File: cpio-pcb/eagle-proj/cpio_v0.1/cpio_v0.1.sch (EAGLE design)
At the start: 2 parts

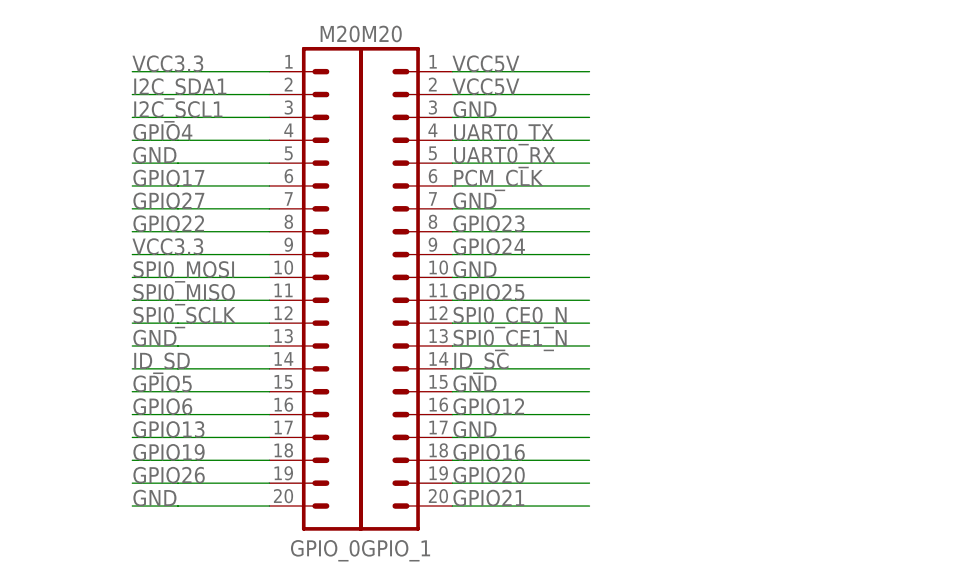
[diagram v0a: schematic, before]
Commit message: schematic update
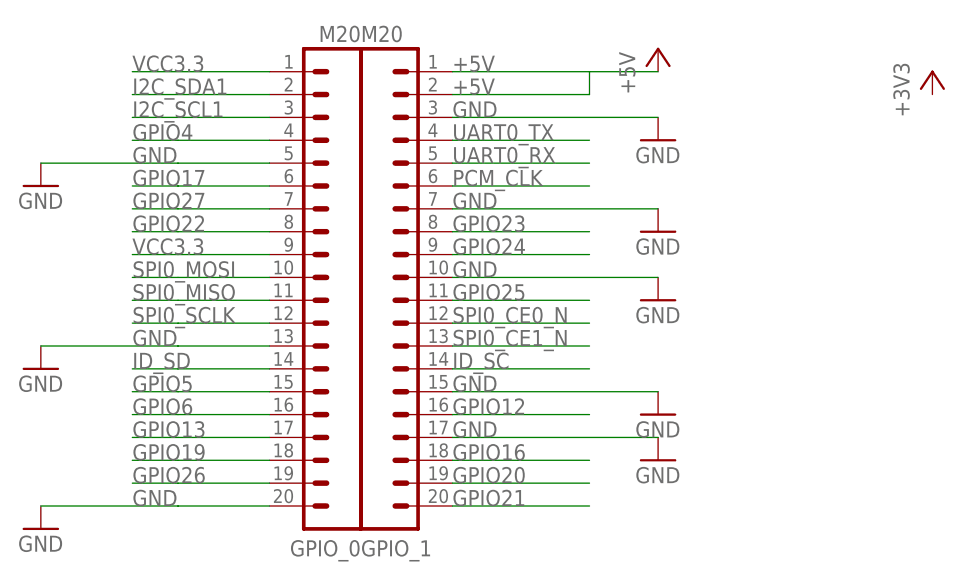
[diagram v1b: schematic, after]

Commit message: clean start with components population of Eagle library
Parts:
- removed GPIO_0, GPIO_1: M20, SparkFun-Connectors:M20
- added JP1: M20X2, SparkFun-Connectors:M20X2
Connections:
- removed net VCC3.3: GPIO_0.1
- new net +5V: JP1.2, JP1.4
- new net GND: JP1.14, JP1.20, JP1.30, JP1.34, JP1.6
- new net GPIO12: JP1.32
- new net GPIO16: JP1.36
- new net GPIO20: JP1.38
- new net GPIO21: JP1.40
- new net GPIO23: JP1.16
- new net GPIO24: JP1.18
- new net GPIO25: JP1.22
- new net ID_SC: JP1.28
- new net PCM_CLK: JP1.12
- new net SPI0_CE0_N: JP1.24
- new net SPI0_CE1_N: JP1.26
- new net UART0_RX: JP1.10
- new net UART0_TX: JP1.8

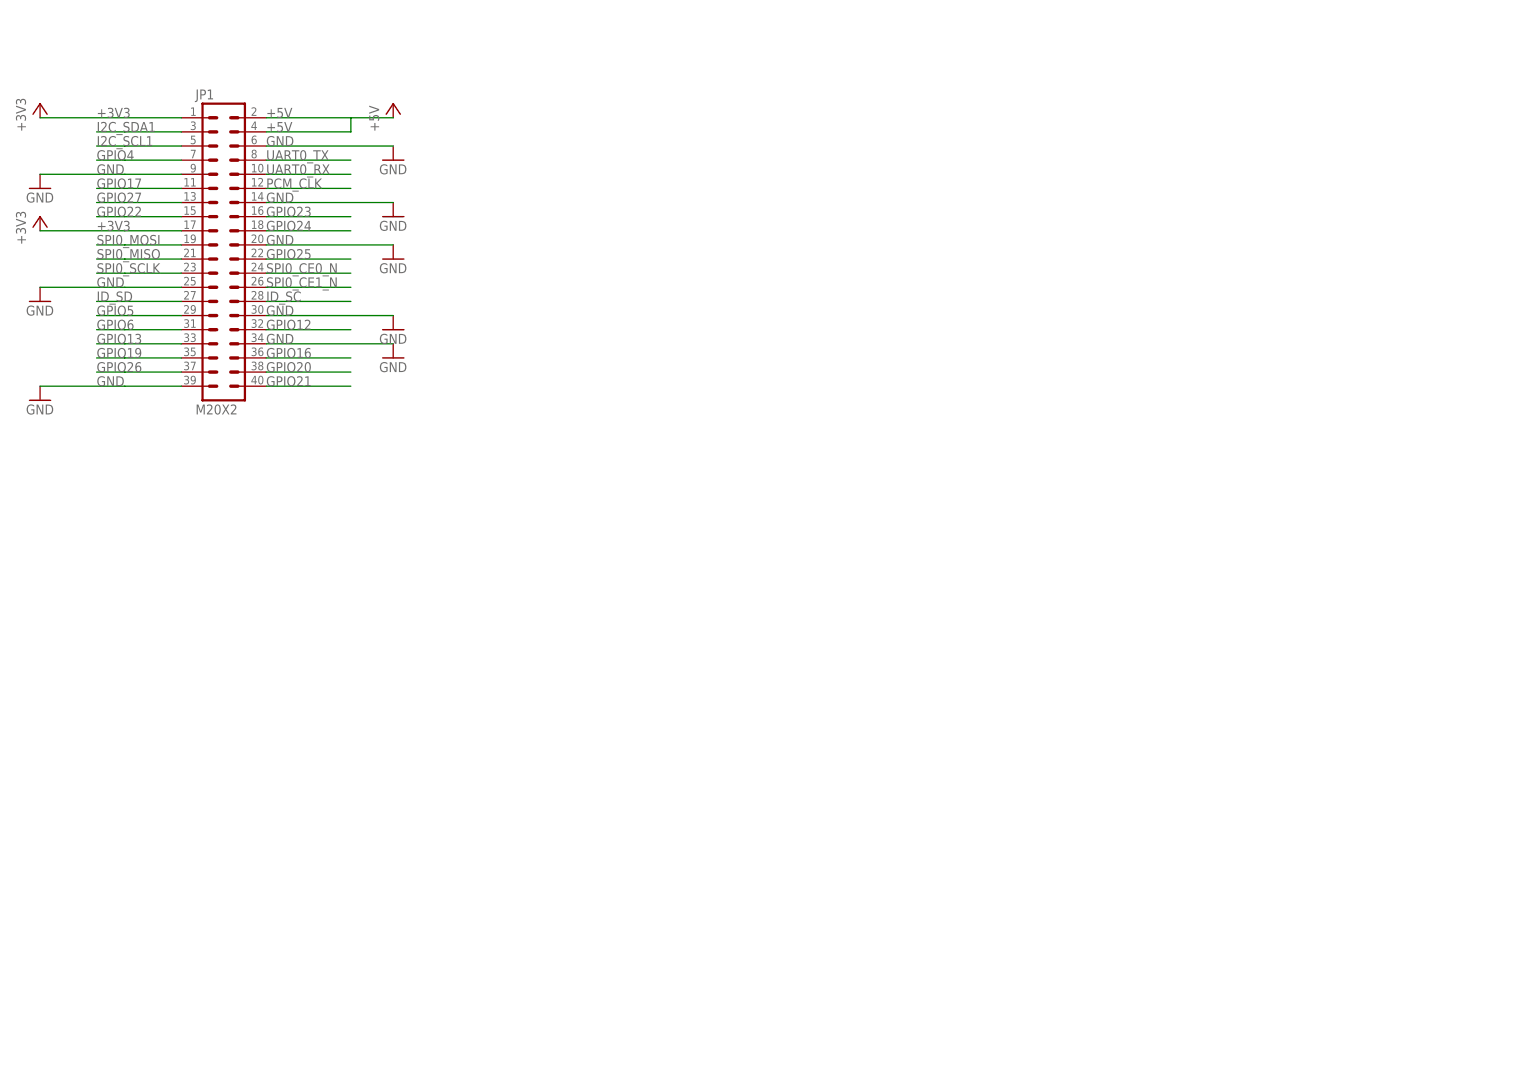
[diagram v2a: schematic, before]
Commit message: schematic for power domains done
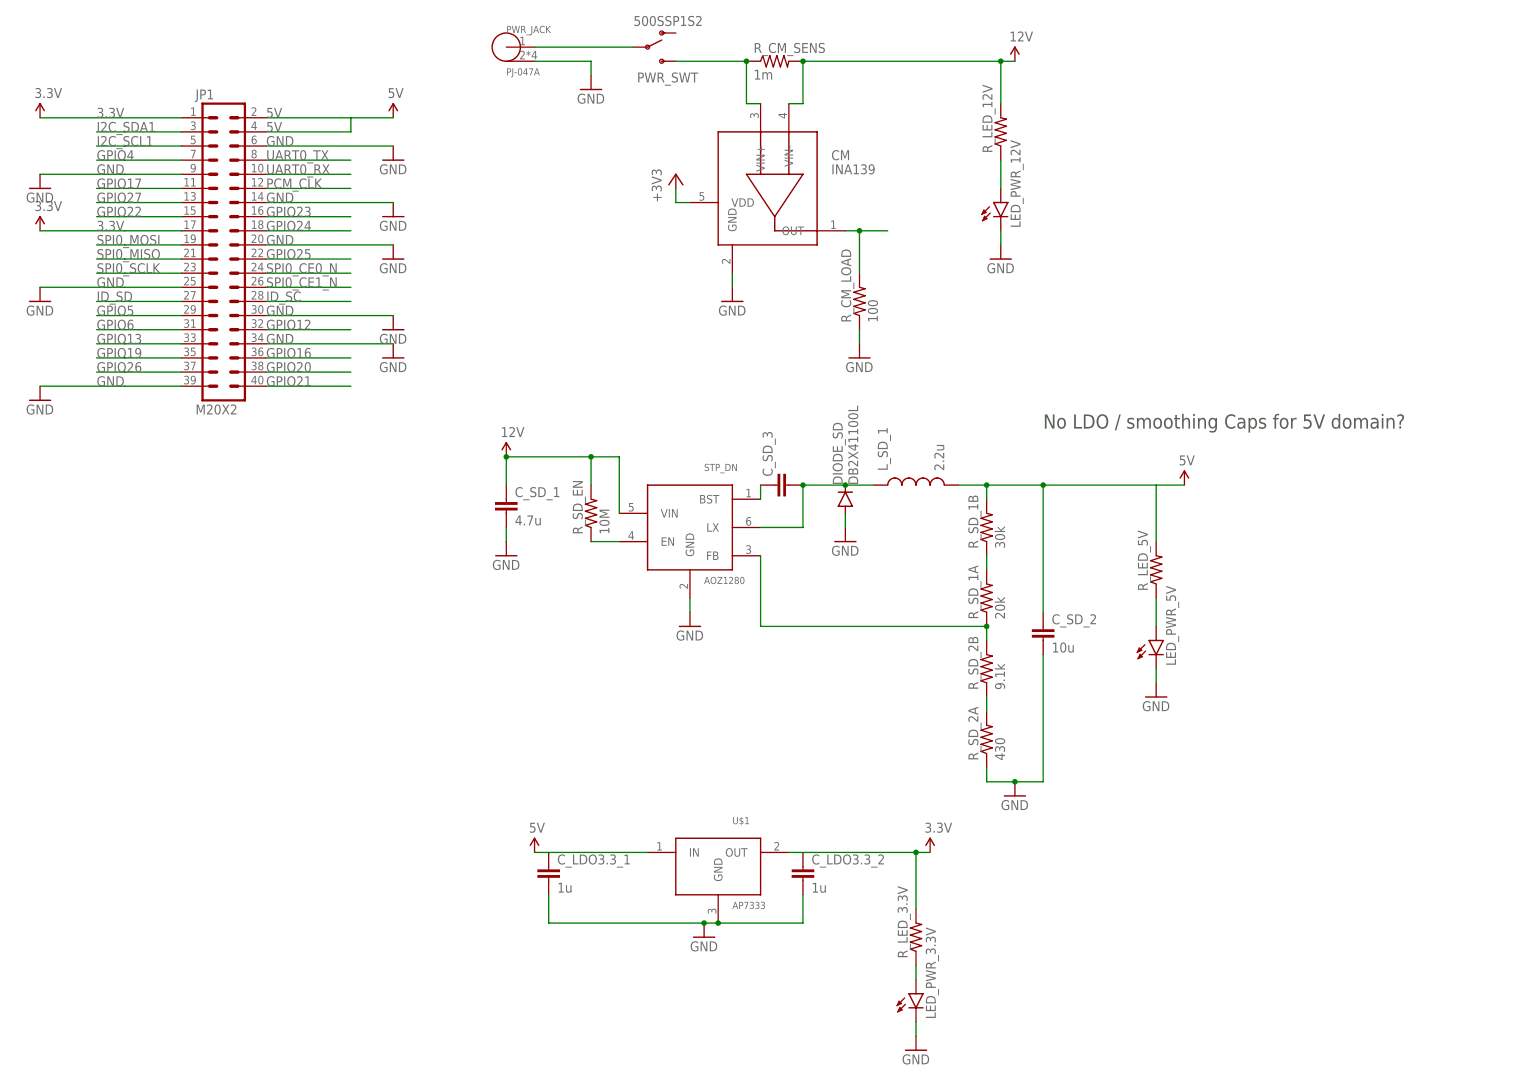
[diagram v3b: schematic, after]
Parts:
- added CM: INA139, cpio:INA139
- added C_LDO3.3_1, C_LDO3.3_2: 1u, SparkFun-Passives:CAP0805
- added C_SD_1: 4.7u, SparkFun-Passives:CAP0805
- added C_SD_2: 10u, SparkFun-Passives:CAP0805
- added C_SD_3: (no value), SparkFun-Passives:CAP0805
- added DIODE_SD: DB2X41100L, cpio:DB2X41100L
- added LED_PWR_12V, LED_PWR_3.3V, LED_PWR_5V: (no value), SparkFun-LED:LED1206
- added L_SD_1: 2.2u, SparkFun-Passives:INDUCTOR0805
- added PWR_JACK: PJ-047A, cpio:PJ-047A
- added PWR_SWT: 500SSP1S2, cpio:500SSP1S2
- added R_CM_LOAD: 100, SparkFun-Passives:RESISTOR0805-RES
- added R_CM_SENS: 1m, SparkFun-Passives:RESISTOR0805-RES
- added R_LED_12V, R_LED_3.3V, R_LED_5V: (no value), SparkFun-Passives:RESISTOR0805-RES
- added R_SD_1A: 20k, SparkFun-Passives:RESISTOR0805-RES
- added R_SD_1B: 30k, SparkFun-Passives:RESISTOR0805-RES
- added R_SD_2A: 430, SparkFun-Passives:RESISTOR0805-RES
- added R_SD_2B: 9.1k, SparkFun-Passives:RESISTOR0805-RES
- added R_SD_EN: 10M, SparkFun-Passives:RESISTOR0805-RES
- added STP_DN: AOZ1280, cpio:AOZ1280
- added U$1: AP7333, cpio:AP7333
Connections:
- removed net +5V: JP1.2, JP1.4
- new net +3V3: CM.VDD
- new net 12V: CM.VIN-, C_SD_1.1, R_CM_SENS.2, R_LED_12V.2, R_SD_EN.2, STP_DN.VIN
- new net 3.3V: R_LED_3.3V.2, U$1.OUT
- new net 5V: C_SD_2.1, JP1.2, JP1.4, L_SD_1.2, R_SD_1B.2, U$1.IN
- new net N$10: C_SD_3.2, DIODE_SD.C, L_SD_1.1, STP_DN.LX
- new net N$11: LED_PWR_5V.A, R_LED_5V.1
- new net N$12: R_SD_1A.1, R_SD_2B.2, STP_DN.FB
- new net N$13: R_SD_2A.2, R_SD_2B.1
- new net N$15: LED_PWR_3.3V.A, R_LED_3.3V.1
- new net N$2: LED_PWR_12V.A, R_LED_12V.1
- new net N$3: PWR_JACK.PWR, PWR_SWT.2
- new net N$4: CM.OUT, R_CM_LOAD.2
- new net N$5: CM.VIN+, PWR_SWT.3, R_CM_SENS.1
- new net N$6: R_SD_EN.1, STP_DN.EN
- new net N$7: R_LED_5V.2
- new net N$8: C_SD_3.1, STP_DN.BST
- new net N$9: R_SD_1A.2, R_SD_1B.1
- net GND: now also CM.GND, C_LDO3.3_1.2, C_LDO3.3_2.2, C_SD_1.2, C_SD_2.2, DIODE_SD.A, LED_PWR_12V.C, LED_PWR_3.3V.C, LED_PWR_5V.C, PWR_JACK.GND, R_CM_LOAD.1, R_SD_2A.1, STP_DN.GND, U$1.GND
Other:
- note added: "No LDO / smoothing Caps for 5V domain?"

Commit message: larger PCB schematic updated, onlyUI missing
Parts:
- added ADC: ADS1115, cpio:ADS1115
- added CAMERA: XH-A-6, cpio:XH-A-6
- added C_ADC: 100n, SparkFun-Passives:CAP0805
- added HEAT_0, HEAT_1, HEAT_2, HEAT_3, SENS_BRIGHT: XH-A-2, cpio:XH-A-2
- added R_1WIRE: 4.7k, SparkFun-Passives:RESISTOR0805-RES
- added R_BRIGHT: (no value), SparkFun-Passives:RESISTOR0805-RES
- added R_HSS_GND, R_SS_PROT0, R_SS_PROT1, R_SS_PROT2, R_SS_PROT3: 1k, SparkFun-Passives:RESISTOR0805-RES
- added R_HSS_PROT_0, R_HSS_PROT_1, R_HSS_PROT_2, R_HSS_PROT_3, R_HSS_SD, R_I2C_0, R_I2C_1, R_SPI_0, R_SPI_1, R_SPI_2, R_SPI_3: 10k, SparkFun-Passives:RESISTOR0805-RES
- added SENS_HUM_0, SENS_HUM_1: XH-A-4, cpio:XH-A-4
- added SENS_TEMP_0, SENS_TEMP_1, SENS_TEMP_2, SENS_TEMP_3: XH-A-3, cpio:XH-A-3
- added SWT_HEAT: VNQ5E160K-E, cpio:VNQ5E160K-E
- added SWT_SENS: 74CBTLV3125, cpio:74CBTLV3125
- renumbered PWR_SWT to SWT_PWR
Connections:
- removed net PCM_CLK: JP1.12
- new net 1WIRE: JP1.12, R_1WIRE.1, SENS_TEMP_0.2, SENS_TEMP_1.2, SENS_TEMP_2.2, SENS_TEMP_3.2
- new net ADC_BRIGHT: ADC.AIN1, R_BRIGHT.1
- new net ADC_PWR: ADC.AIN0, CM.OUT, R_CM_LOAD.2
- new net I2C_SCL: ADC.SCL, R_I2C_0.1, SENS_HUM_0.2, SENS_HUM_1.2
- new net I2C_SDA: ADC.SDA, R_I2C_1.1, SENS_HUM_0.3, SENS_HUM_1.3
- new net N$1: JP1.11, JP1.13, JP1.15, JP1.19, JP1.21, JP1.23, JP1.25, JP1.27, JP1.29, JP1.3, JP1.31, JP1.33, JP1.35, JP1.37, JP1.39, JP1.5, JP1.7, JP1.9
- new net N$14: R_SS_PROT0.2, SWT_SENS.1OE
- new net N$16: SENS_TEMP_1.1, SWT_SENS.2B
- new net N$17: SENS_TEMP_0.1, SWT_SENS.1B
- new net N$18: SENS_TEMP_2.1, SWT_SENS.3B
- new net N$19: SENS_TEMP_3.1, SWT_SENS.4B
- new net N$20: R_SS_PROT1.2, SWT_SENS.2OE
- new net N$21: R_SS_PROT2.2, SWT_SENS.3OE
- new net N$22: R_SS_PROT3.2, SWT_SENS.4OE
- new net N$24: ADC.AIN2
- new net N$25: ADC.AIN3
- new net N$26: HEAT_2.1, SWT_HEAT.OUTPUT3
- new net N$27: HEAT_1.1, SWT_HEAT.OUTPUT2
- new net N$28: HEAT_0.1, SWT_HEAT.OUTPUT1
- new net N$29: HEAT_3.1, SWT_HEAT.OUTPUT4
- new net N$30: R_HSS_SD.1, SWT_HEAT.STAT_DIS
- new net N$31: R_HSS_PROT_3.2, SWT_HEAT.INPUT4
- new net N$32: R_HSS_PROT_2.2, SWT_HEAT.INPUT3
- new net N$33: R_HSS_PROT_1.2, SWT_HEAT.INPUT2
- new net N$34: R_HSS_PROT_0.2, SWT_HEAT.INPUT1
- new net N$35: R_BRIGHT.2, SENS_BRIGHT.1
- new net SPI0_MISO: CAMERA.4, R_SPI_1.1
- new net SPI0_MOSI: CAMERA.3, R_SPI_2.1
- new net SPI0_SCLK: CAMERA.2, R_SPI_0.1
- net 12V: now also SWT_HEAT.VCC
- net 3.3V: now also ADC.VDD, CAMERA.1, C_ADC.2, JP1.1, JP1.17, R_1WIRE.2, R_HSS_SD.2, R_I2C_0.2, R_I2C_1.2, R_SPI_0.2, R_SPI_1.2, R_SPI_2.2, R_SPI_3.2, SENS_HUM_0.1, SENS_HUM_1.1, SWT_SENS.1A, SWT_SENS.2A, SWT_SENS.3A, SWT_SENS.4A, SWT_SENS.VCC
- net GND: now also ADC.ADDR, ADC.GND, CAMERA.6, C_ADC.1, HEAT_0.2, HEAT_1.2, HEAT_2.2, HEAT_3.2, R_HSS_GND.2, SENS_BRIGHT.2, SENS_HUM_0.4, SENS_HUM_1.4, SENS_TEMP_0.3, SENS_TEMP_1.3, SENS_TEMP_2.3, SENS_TEMP_3.3, SWT_SENS.GND
- net N$4: now also R_HSS_GND.1, SWT_HEAT.GND; no longer CM.OUT, R_CM_LOAD.2
- net SPI0_CE0_N: now also CAMERA.5, R_SPI_3.1
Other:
- note added: "DeCap?!"
- note added: "Ground Diode missing!"
- note added: "Load Diode missing!"
- note added: "Plugs for potential pH Sensors missing!"
- note added: "open"
- moved on the sheet: JP1
